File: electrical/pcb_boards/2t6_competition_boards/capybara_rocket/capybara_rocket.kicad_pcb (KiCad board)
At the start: 4 copper layers, 145 x 65 mm, 56 parts, among them J1 SparkFun MAX-M10S, J10 Wurth_M4_62000411622, J11 Wurth_M4_62000411622, J12 Wurth_M3_62000311622, J13 Wurth_M3_62000311622, J14 Wurth_M3_62000311622, J15 Wurth_M3_62000311622, J16 Wurth_M3_62000311622, J17 Wurth_M3_62000311622, J2 VL53L1-SATEL, J3 Wurth_M2_62000211622, J4 Wurth_M2_62000211622, J5 Wurth_M2_62000211622, J6 Wurth_M2_62000211622, J7 Wurth_M2_62000211622, J9 Wurth_M4_62000411622, U1 WRL-11812, U10 MAX756CPA_, U11 LTC3536EMSE_PBF, U12 MP3414AGJ-Z, U13 Adafruit BMP581, U14 INA219BIDR, U2 Adafruit BNO085, U4 STM32 NUCLEO-G431KB, U5 DS1307+, U6 NE555P, U7 25LC1024-E/P, U8 DRV8212DRLR, U9 SN74LVC1G04DBVR, Y1 AB38T-32.768KHZ

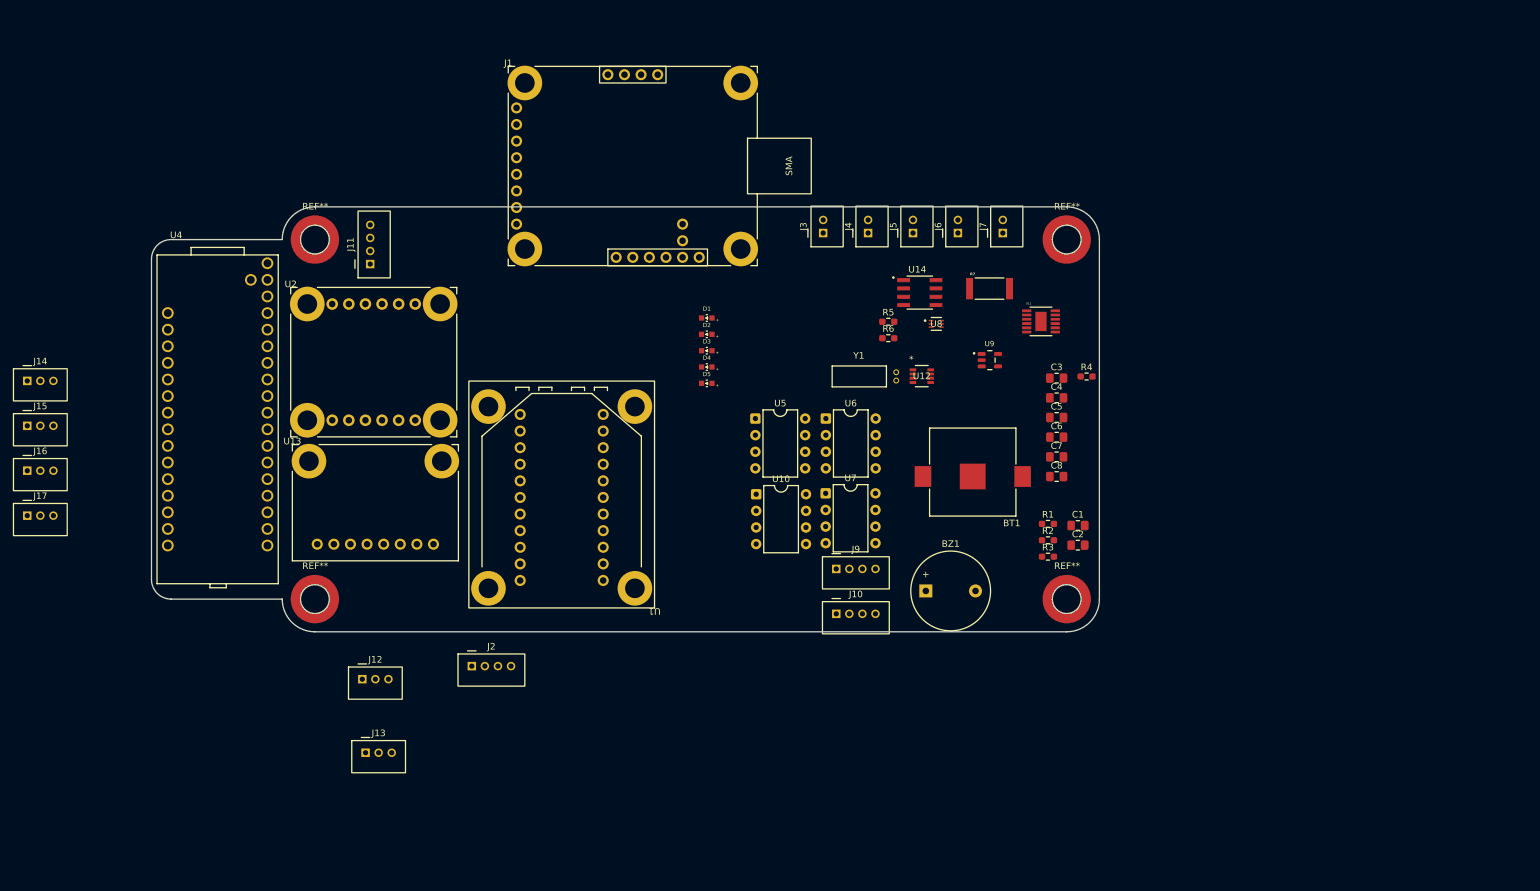
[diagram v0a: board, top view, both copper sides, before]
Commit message: Adding BMP581 KiCad models and big boi updates to CPL PCB
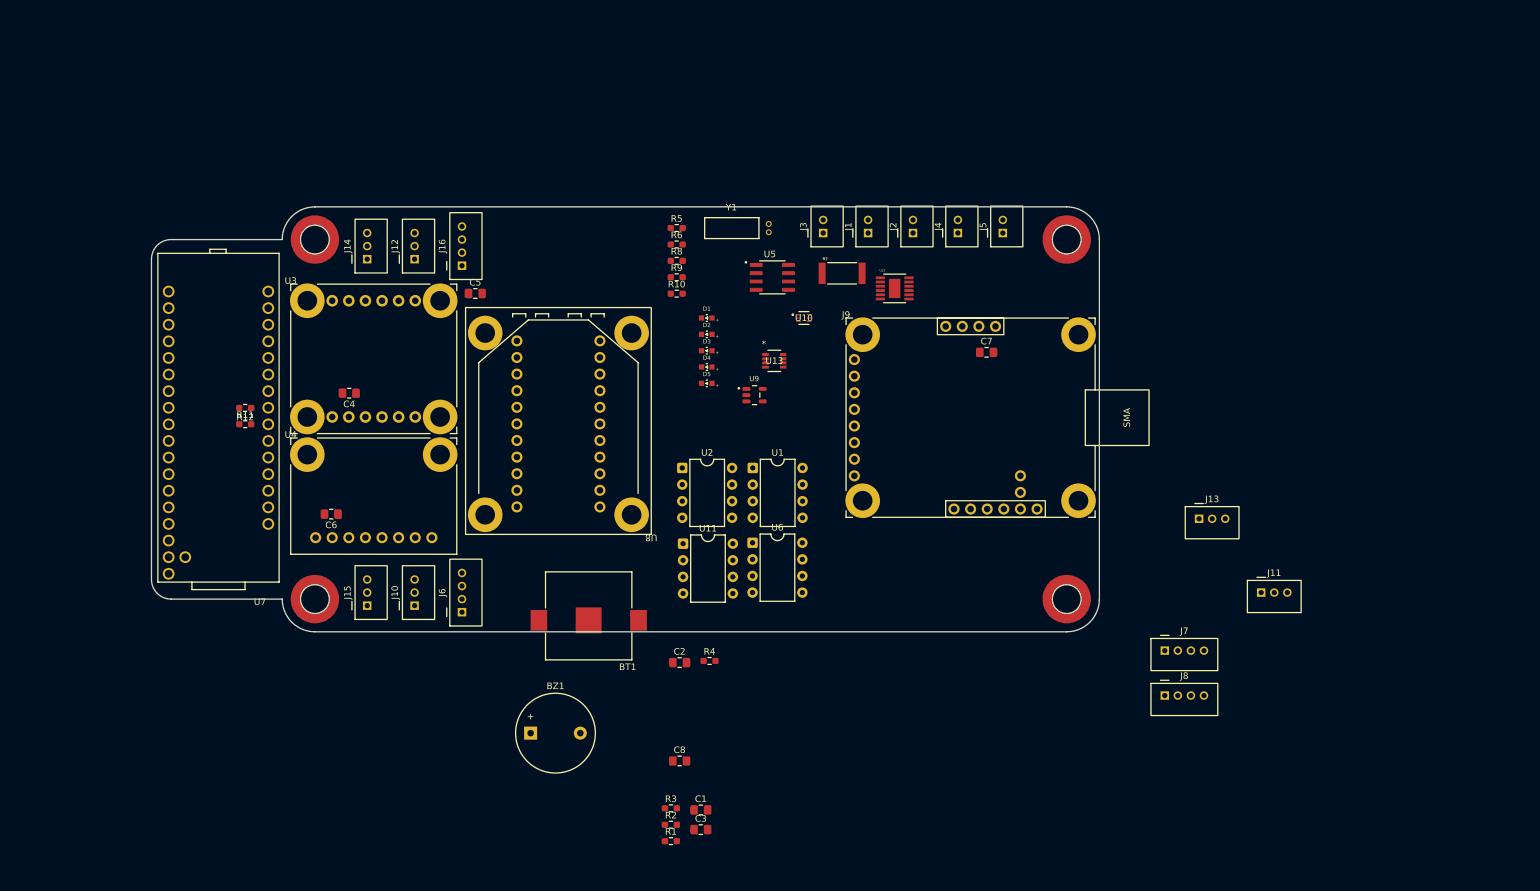
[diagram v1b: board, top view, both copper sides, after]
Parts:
- removed the J11 at (111.0, 76.2)
- removed the U13 at (99.0, 103.9)
- added J16: DC Motor, RSX_CanSat_Custom_KiCad_Footprints:J_Wurth_WR-WTB_62000411622, F.Cu at (125.0, 76.5)
- added R10: 100Ω, Resistor_SMD:R_0603_1608Metric_Pad0.98x0.95mm_HandSolder, F.Cu at (157.8, 80.8)
- added R5: 100Ω, Resistor_SMD:R_0603_1608Metric_Pad0.98x0.95mm_HandSolder, F.Cu at (157.8, 70.7)
- added R6: 100Ω, Resistor_SMD:R_0603_1608Metric_Pad0.98x0.95mm_HandSolder, F.Cu at (157.8, 73.2)
- added R8: 100Ω, Resistor_SMD:R_0603_1608Metric_Pad0.98x0.95mm_HandSolder, F.Cu at (157.8, 75.8)
- added R9: 100Ω, Resistor_SMD:R_0603_1608Metric_Pad0.98x0.95mm_HandSolder, F.Cu at (157.8, 78.3)
- added U4: Adafruit BMP581, RSX_CanSat_Custom_KiCad_Footprints:Adafruit_BMP581, F.Cu at (98.8, 102.9)
- J10: renamed from J12; value Wurth_M3_62000311622 -> Servo NC
- J11: renamed from J13; value Wurth_M3_62000311622 -> Servo CC
- J12: renamed from J14; value Wurth_M3_62000311622 -> Servo EGG
- J13: renamed from J15; value Wurth_M3_62000311622 -> Servo ELEVATOR
- J14: renamed from J16; value Wurth_M3_62000311622 -> Servo AILERON 1
- J15: renamed from J17; value Wurth_M3_62000311622 -> Servo AILERON 2
- J3: value Wurth_M2_62000211622 -> LED
- J7: renamed from J9; value Wurth_M4_62000411622 -> Ground Camera
- J8: renamed from J10; value Wurth_M4_62000411622 -> Payload Camera
- U5: renamed from U14; value INA219BIDR -> INA219
- U6: renamed from U7; value 25LC1024-E/P -> EEPROM
- U8: renamed from U1; value WRL-11812 -> SparkFun XBee Explorer
- moved J13 179.8 mm to (237.8, 115.2)
- moved J11 139.2 mm to (247.2, 126.5)
- moved C6 111.6 mm to (105.0, 114.5), turned to 180 degrees
- moved C4 108.2 mm to (107.8, 96.0), turned to 180 degrees
- moved R11 99.6 mm to (91.8, 100.8)
- moved R12 99.0 mm to (91.8, 98.2), turned to 180 degrees
- moved C5 90.9 mm to (127.0, 80.8)
- moved C1 72.2 mm to (161.5, 159.8)
- moved C2 72.2 mm to (158.3, 137.2)
- moved C3 72.2 mm to (161.5, 162.8)
- moved C8 72.2 mm to (158.3, 152.3)
- moved R1 72.2 mm to (157.0, 164.5)
- moved R2 72.2 mm to (157.0, 162.0)
- moved R3 72.2 mm to (157.0, 159.5)
- moved R4 72.2 mm to (162.9, 137.0)
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- renumbered C3 to C2, C2 to C3, J4 to J1, J5 to J2, J6 to J4, J7 to J5, J2 to J6, J1 to J9, R3 to R1, R5 to R11, R6 to R12, R1 to R3, U6 to U1, U8 to U10, U10 to U11, U11 to U12, U12 to U13, U5 to U2, U2 to U3, U4 to U7
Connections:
- D1 pad 1: unconnected-(D1-K-Pad1) -> GND
- D1 pad 2: unconnected-(D1-A-Pad2) -> Net-(D1-A)
- D2 pad 1: unconnected-(D2-K-Pad1) -> GND
- D2 pad 2: unconnected-(D2-A-Pad2) -> Net-(D2-A)
- D3 pad 1: unconnected-(D3-K-Pad1) -> GND
- D3 pad 2: unconnected-(D3-A-Pad2) -> Net-(D3-A)
- D4 pad 1: unconnected-(D4-K-Pad1) -> GND
- D4 pad 2: unconnected-(D4-A-Pad2) -> Net-(D4-A)
- D5 pad 1: unconnected-(D5-K-Pad1) -> GND
- D5 pad 2: unconnected-(D5-A-Pad2) -> Net-(D5-A)
- J10 pad 1: unconnected-(J12-Pad1) -> GND
- J10 pad 2: unconnected-(J12-Pad2) -> NC_REL
- J10 pad 3: unconnected-(J12-Pad3) -> 5V
- J11 pad 1: unconnected-(J13-Pad1) -> GND
- J11 pad 2: unconnected-(J13-Pad2) -> CC_REL
- J11 pad 3: unconnected-(J13-Pad3) -> 5V
- J12 pad 1: unconnected-(J14-Pad1) -> GND
- J12 pad 2: unconnected-(J14-Pad2) -> EGG_REL
- J12 pad 3: unconnected-(J14-Pad3) -> 5V
- J13 pad 1: unconnected-(J15-Pad1) -> GND
- J13 pad 2: unconnected-(J15-Pad2) -> ELEVATOR
- J13 pad 3: unconnected-(J15-Pad3) -> 5V
- J14 pad 1: unconnected-(J16-Pad1) -> GND
- J14 pad 2: unconnected-(J16-Pad2) -> AILERON
- J14 pad 3: unconnected-(J16-Pad3) -> 5V
- J15 pad 1: unconnected-(J17-Pad1) -> GND
- J15 pad 2: unconnected-(J17-Pad2) -> AILERON
- J15 pad 3: unconnected-(J17-Pad3) -> 5V
- J6 pad 2: 3.3V -> SDA
- J6 pad 3: SDA -> SCL
- J6 pad 4: SCL -> 3.3V
- J7 pad 1: unconnected-(J9-Pad1) -> GND
- J7 pad 2: unconnected-(J9-Pad2) -> G_CAM_IN
- J7 pad 3: unconnected-(J9-Pad3) -> G_CAM_OUT
- J7 pad 4: unconnected-(J9-Pad4) -> 5V
- J8 pad 1: unconnected-(J10-Pad1) -> GND
- J8 pad 2: unconnected-(J10-Pad2) -> PG_CAM_IN
- J8 pad 3: unconnected-(J10-Pad3) -> PG_CAM_OUT
- J8 pad 4: unconnected-(J10-Pad4) -> 5V
- R7 pad 1: Net-(U14-VIN-) -> 3.3V
- U5 pad 7: Net-(U14-VIN-) -> 3.3V
- U6 pad 1: unconnected-(U7-*CS-Pad1) -> CS
- U6 pad 2: unconnected-(U7-SO-Pad2) -> MISO
- U6 pad 3: unconnected-(U7-*WP-Pad3) -> GND
- U6 pad 4: unconnected-(U7-VSS-Pad4) -> GND
- U6 pad 5: unconnected-(U7-SI-Pad5) -> MOSI
- U6 pad 6: unconnected-(U7-SCK-Pad6) -> SCLK
- U6 pad 7: unconnected-(U7-*HOLD-Pad7) -> 3.3V
- U6 pad 8: unconnected-(U7-VCC-Pad8) -> 3.3V

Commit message: March 15 CPL PCB update
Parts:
- J1: value Wurth_M2_62000211622 -> 3.6V Battery
- J10: renamed from J13; value Servo ELEVATOR -> Elevator
- J12: renamed from J14; value Servo AILERON 1 -> Aileron 1
- J13: renamed from J15; value Servo AILERON 2 -> Aileron 2
- J2: renamed from J4; value Wurth_M2_62000211622 -> 1.2V Battery
- J3: renamed from J2; value Wurth_M2_62000211622 -> 3.6V Switch
- J4: renamed from J5; value Wurth_M2_62000211622 -> 1.2V Switch
- J6: renamed from J10; value Servo NC -> NC
- J7: renamed from J11; value Servo CC -> CC
- J9: renamed from J12; value Servo EGG -> Egg
- moved J4 10.5 mm to (208.8, 61.0)
- moved U3 0.50 mm to (98.3, 79.3)
- moved U6 0.50 mm to (98.3, 102.9)
- renumbered J9 to J11, J7 to J14, J16 to J15, J8 to J16, J3 to J5, J6 to J8, R8 to R10, R9 to R11, R10 to R12, R7 to R5, R11 to R6, R12 to R7, R5 to R8, R6 to R9, U11 to U10, U6 to U11, U7 to U12, U8 to U13, U10 to U4, U9 to U5, U4 to U6, U12 to U7, U13 to U8, U5 to U9
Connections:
- J1 pad 1: 5V -> GND
- J1 pad 2: GND -> 3.6V
- J2 pad 1: unconnected-(J4-Pad1) -> GND
- J2 pad 2: unconnected-(J4-Pad2) -> 1.2V
- J3 pad 1: 5V -> GND
- J3 pad 2: GND -> 3.6V
- J4 pad 1: unconnected-(J5-Pad1) -> GND
- J4 pad 2: unconnected-(J5-Pad2) -> 1.2V
- J5 pad 1: Net-(J3-Pad1) -> GND
- J5 pad 2: GND -> Net-(J5-Pad2)
- R4 pad 1: Net-(J3-Pad1) -> Net-(J5-Pad2)
- R4 pad 2: unconnected-(R4-Pad2) -> 3.3V
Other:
- outline, holes or cut-outs redrawn

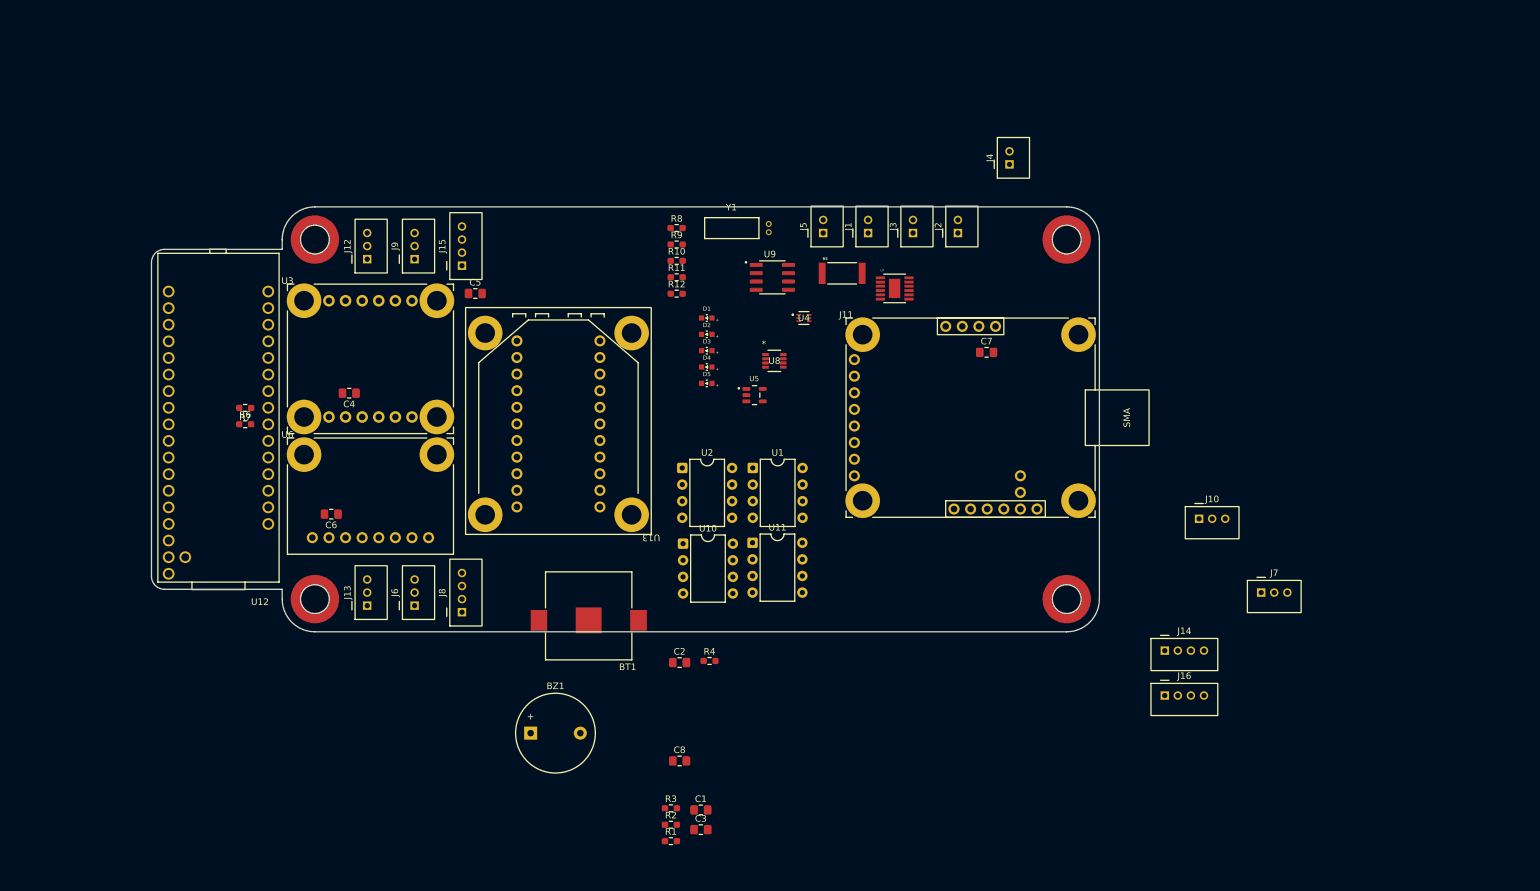
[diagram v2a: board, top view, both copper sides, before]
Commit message: LT3536 and MP3414 circuit design
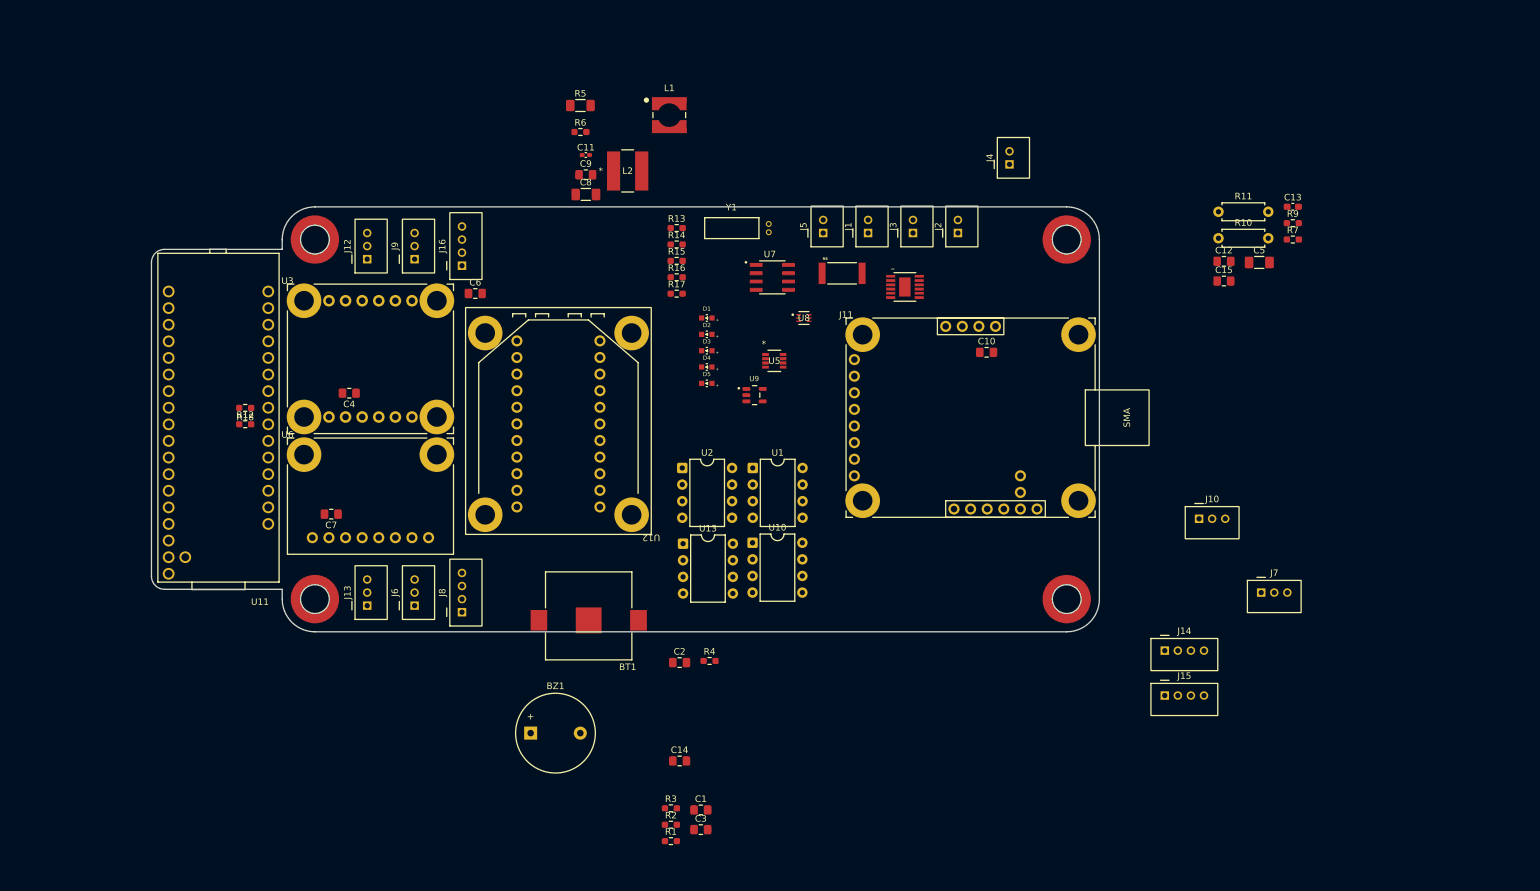
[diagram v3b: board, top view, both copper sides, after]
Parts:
- added C11: 1μF, Capacitor_SMD:C_0402_1005Metric_Pad0.74x0.62mm_HandSolder, F.Cu at (143.9, 59.6)
- added C12: 220pF, Capacitor_SMD:C_0805_2012Metric_Pad1.18x1.45mm_HandSolder, F.Cu at (241.5, 75.8)
- added C13: 47pF, Capacitor_SMD:C_0603_1608Metric_Pad1.08x0.95mm_HandSolder, F.Cu at (252.1, 67.5)
- added C15: 22μF, Capacitor_SMD:C_0805_2012Metric_Pad1.18x1.45mm_HandSolder, F.Cu at (241.5, 78.8)
- added C5: 10μF, Capacitor_SMD:C_1206_3216Metric_Pad1.33x1.80mm_HandSolder, F.Cu at (247.0, 76.0)
- added C8: 10μF, Capacitor_SMD:C_1206_3216Metric_Pad1.33x1.80mm_HandSolder, F.Cu at (143.9, 65.6)
- added C9: 22μF, Capacitor_SMD:C_0805_2012Metric_Pad1.18x1.45mm_HandSolder, F.Cu at (143.9, 62.6)
- added L1: 15μH, RSX_CanSat_Custom_KiCad_Footprints:WE-TPC_4828, F.Cu at (156.7, 53.5)
- added L2: 2.2μH, RSX_CanSat_Custom_KiCad_Footprints:IND_BOURNS_SRN6045, F.Cu at (150.3, 62.0)
- added R10: 221kΩ, Resistor_THT:R_Axial_DIN0207_L6.3mm_D2.5mm_P7.62mm_Horizontal, F.Cu at (240.7, 72.3)
- added R11: 1MΩ, Resistor_THT:R_Axial_DIN0207_L6.3mm_D2.5mm_P7.62mm_Horizontal, F.Cu at (240.7, 68.2)
- added R5: 61.9kΩ, Resistor_SMD:R_1206_3216Metric_Pad1.30x1.75mm_HandSolder, F.Cu at (143.1, 52.0)
- added R6: 505kΩ, Resistor_SMD:R_0603_1608Metric_Pad0.98x0.95mm_HandSolder, F.Cu at (143.1, 56.0)
- added R7: 51kΩ, Resistor_SMD:R_0603_1608Metric_Pad0.98x0.95mm_HandSolder, F.Cu at (252.1, 72.5)
- added R9: 6.2kΩ, Resistor_SMD:R_0603_1608Metric_Pad0.98x0.95mm_HandSolder, F.Cu at (252.1, 70.0)
- U4: renamed from U7; value LTC3536EMSE_PBF -> LTC3536
- U5: renamed from U8; value MP3414AGJ-Z -> MP3414
- moved U4 1.58 mm to (192.8, 79.8)
- renumbered C7 to C10, C8 to C14, C5 to C6, C6 to C7, J16 to J15, J15 to J16, R6 to R12, R8 to R13, R9 to R14, R10 to R15, R11 to R16, R12 to R17, R7 to R18, R5 to R8, U11 to U10, U12 to U11, U13 to U12, U10 to U13, U9 to U7, U4 to U8, U5 to U9
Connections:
- net 3.6V renamed 3.6V+
- C2 pad 1: 5V -> 5.5V
- J10 pad 3: 5V -> 5.5V
- J12 pad 3: 5V -> 5.5V
- J13 pad 3: 5V -> 5.5V
- J14 pad 4: 5V -> 5.5V
- J15 pad 4: 5V -> 5.5V
- J16 pad 4: 5V -> 5.5V
- J6 pad 3: 5V -> 5.5V
- J7 pad 3: 5V -> 5.5V
- J9 pad 3: 5V -> 5.5V
- R8 pad 1: 3.3V -> 3.6V-
- U2 pad 8: 5V -> 5.5V
- U4 pad 1: unconnected-(U7-RT-Pad1) -> 3.6V-
- U4 pad 11: unconnected-(U7-FB-Pad11) -> Net-(U4-FB)
- U4 pad 12: unconnected-(U7-VC-Pad12) -> Net-(U4-VC)
- U4 pad 2: unconnected-(U7-SGND-Pad2) -> GND
- U4 pad 4: unconnected-(U7-SW1-Pad4) -> Net-(U4-SW1)
- U4 pad 5: unconnected-(U7-PGND-Pad5) -> GND
- U4 pad 6: unconnected-(U7-SW2-Pad6) -> Net-(U4-SW2)
- U4 pad 7: unconnected-(U7-VOUT-Pad7) -> 3.3V
- U4 pad 9: unconnected-(U7-VIN-Pad9) -> 3.6V-
- U5 pad 1: unconnected-(U8-IN-Pad1) -> 3.6V-
- U5 pad 2: unconnected-(U8-OUT-Pad2) -> 5.5V
- U5 pad 3: unconnected-(U8-SW-Pad3) -> Net-(U5-SW)
- U5 pad 4: unconnected-(U8-PGND-Pad4) -> GND
- U5 pad 6: unconnected-(U8-AGND-Pad6) -> GND
- U5 pad 7: unconnected-(U8-FB-Pad7) -> Net-(U5-FB)
- U7 pad 7: 3.3V -> 3.6V-

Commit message: MAX756 circuit design
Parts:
- added C16: 150μF, Capacitor_THT:CP_Radial_D6.3mm_P2.50mm, F.Cu at (198.0, 132.7)
- added C17: 100μF, Capacitor_THT:CP_Radial_D8.0mm_P3.50mm, F.Cu at (188.7, 133.6)
- added D6: 1N5820, Diode_THT:D_DO-201AD_P15.24mm_Horizontal, F.Cu at (187.8, 125.4)
- added L3: 22μH, RSX_CanSat_Custom_KiCad_Footprints:IND_CD54_SUM, F.Cu at (199.1, 140.2)
- U13: value MAX756CPA_ -> MAX756CPA+
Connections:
- R13 pad 2: unconnected-(R13-Pad2) -> 5.5V
- R14 pad 2: unconnected-(R14-Pad2) -> 5V
- R15 pad 2: unconnected-(R15-Pad2) -> 3.3V
- R16 pad 2: unconnected-(R16-Pad2) -> 3.6V+
- R17 pad 2: unconnected-(R17-Pad2) -> 1.2V
- U13 pad 5: unconnected-(U13-LBI-Pad5) -> 1.2V
- U13 pad 6: unconnected-(U13-OUT-Pad6) -> Net-(D6-K)
- U13 pad 7: unconnected-(U13-GND-Pad7) -> GND
- U13 pad 8: unconnected-(U13-LX-Pad8) -> Net-(D6-A)
